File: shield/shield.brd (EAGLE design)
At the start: 102.5 x 66 mm, 4 parts, among them IC1 LM73

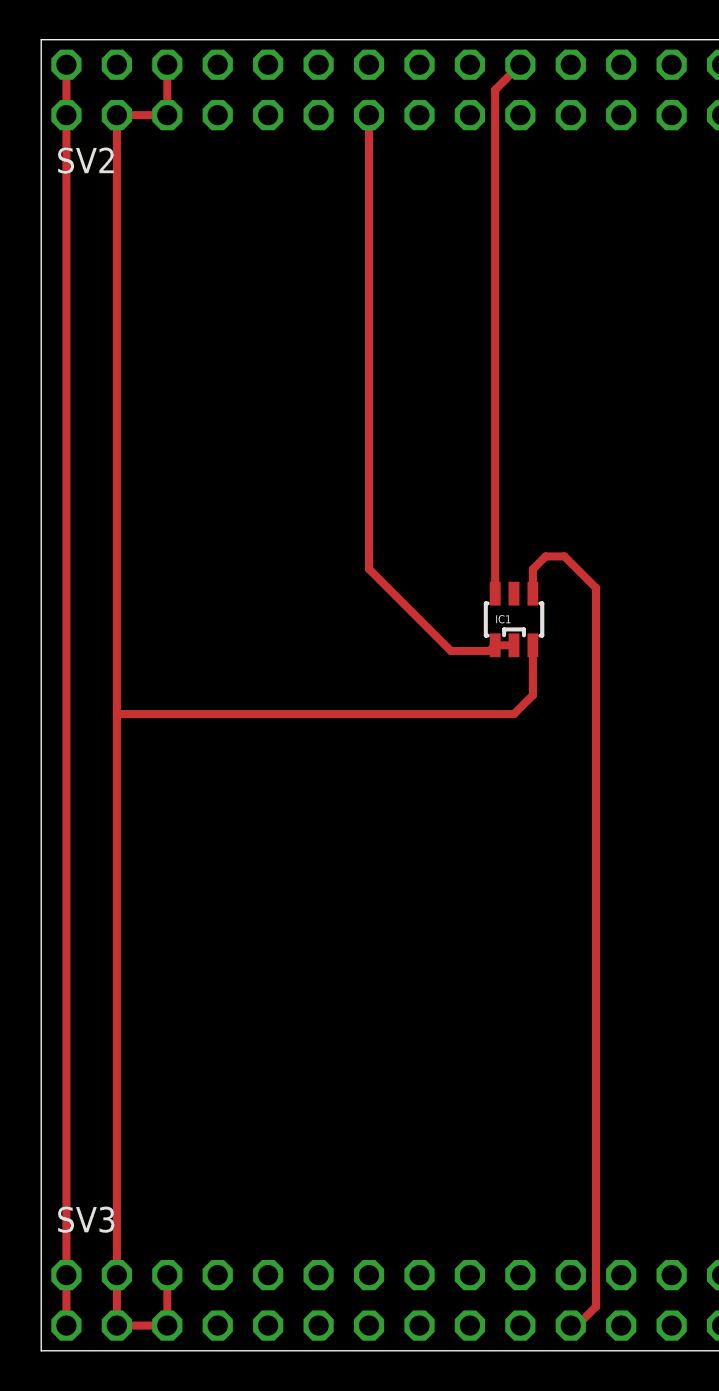
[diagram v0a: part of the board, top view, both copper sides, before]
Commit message: remove lm73 from shield
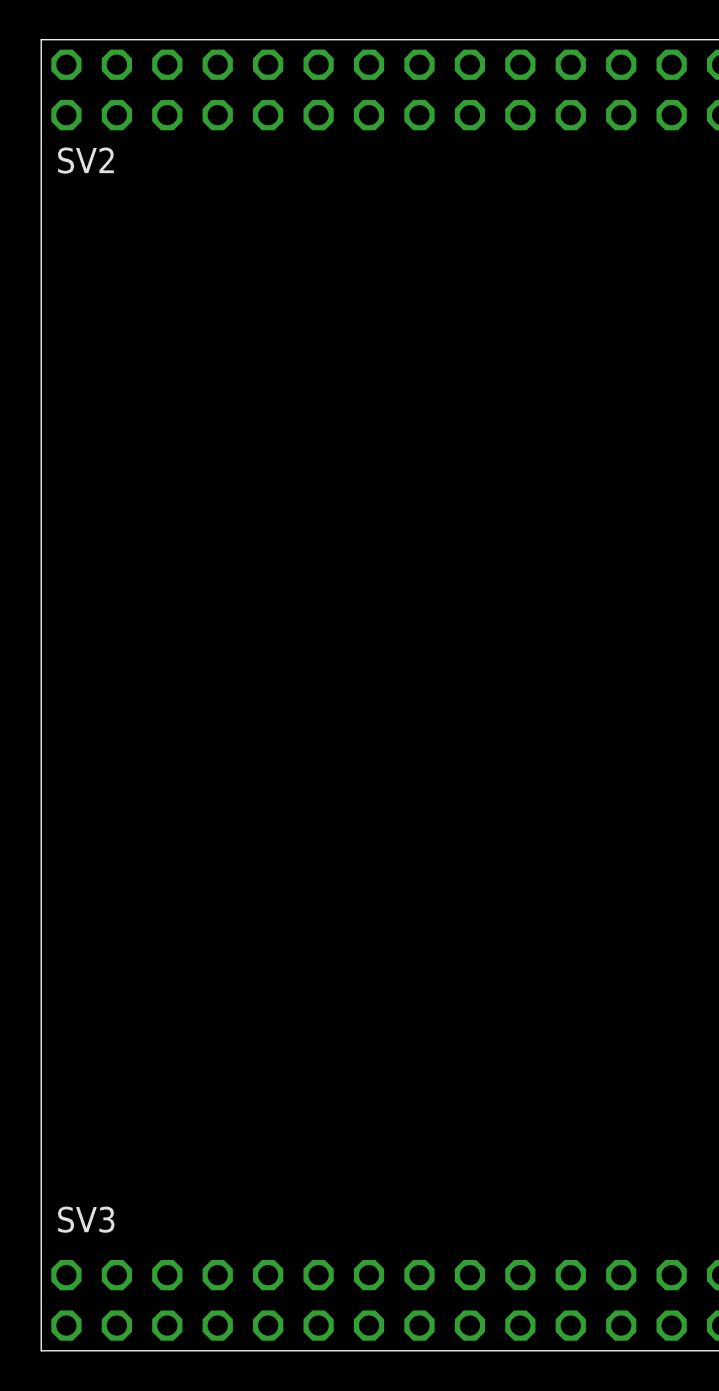
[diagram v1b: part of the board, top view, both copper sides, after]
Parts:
- removed IC1: LM73, boomerang:SOT23-6
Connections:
- net +3V3: no longer IC1.3
- net GND: no longer IC1.1, IC1.2
- net P40: no longer IC1.6
- net P41: no longer IC1.4
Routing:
- net +3V3: track 95.0 -> 0.00 mm
- net +5V: track 63.5 -> 0.00 mm
- net P41: track 43.2 -> 0.00 mm
- net GND: track 32.0 -> 0.00 mm
- net P40: track 27.2 -> 0.00 mm
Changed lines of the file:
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@@
 <attribute name="VALUE" x="93.98" y="18.161" size="1.27" layer="28" ratio="10" rot="MR180"/>
 </element>
-<element name="IC1" library="boomerang" package="SOT23-6" value="LM73" x="22.5425" y="48.26"/>
 </elements>
 <signals>
@@
 <contactref element="SV2" pad="57"/>
 <contactref element="SV2" pad="79"/>
-<contactref element="IC1" pad="1"/>
-<contactref element="IC1" pad="2"/>
 <wire x1="88.9" y1="73.66" x2="99.06" y2="76.2" width="0" layer="19" extent="1-1"/>
 <wire x1="71.12" y1="76.2" x2="88.9" y2="73.66" width="0" layer="19" extent="1-1"/>
@@
 <wire x1="43.18" y1="15.24" x2="68.58" y2="15.24" width="0" layer="19" extent="1-1"/>
 <wire x1="22.86" y1="15.24" x2="43.18" y2="15.24" width="0" layer="19" extent="1-1"/>
-<wire x1="15.24" y1="73.66" x2="15.24" y2="50.8" width="0.4064" layer="1"/>
-<wire x1="15.24" y1="50.8" x2="19.3675" y2="46.6725" width="0.4064" layer="1"/>
-<wire x1="19.3675" y1="46.6725" x2="21.3051" y2="46.6725" width="0.4064" layer="1"/>
-<wire x1="21.3051" y1="46.6725" x2="21.5925" y2="46.9599" width="0.4064" layer="1"/>
-<wire x1="21.5925" y1="46.9599" x2="22.5425" y2="46.9599" width="0.4064" layer="1"/>
 </signal>
 <signal name="P14">
@@
 <signal name="P40">
 <contactref element="SV2" pad="19"/>
-<contactref element="IC1" pad="6"/>
-<wire x1="21.5925" y1="49.5601" x2="21.5925" y2="74.9325" width="0.4064" layer="1"/>
-<wire x1="21.5925" y1="74.9325" x2="22.86" y2="76.2" width="0.4064" layer="1"/>
 </signal>
 <signal name="P36">
@@
 <signal name="P41">
 <contactref element="SV3" pad="22"/>
-<contactref element="IC1" pad="4"/>
-<wire x1="23.4925" y1="49.5601" x2="23.4925" y2="50.7975" width="0.4064" layer="1"/>
-<wire x1="23.4925" y1="50.7975" x2="24.13" y2="51.435" width="0.4064" layer="1"/>
-<wire x1="24.13" y1="51.435" x2="25.0825" y2="51.435" width="0.4064" layer="1"/>
-<wire x1="25.4" y1="12.7" x2="25.7175" y2="12.7" width="0.4064" layer="1"/>
-<wire x1="25.7175" y1="12.7" x2="26.67" y2="13.6525" width="0.4064" layer="1"/>
-<wire x1="26.67" y1="13.6525" x2="26.67" y2="49.8475" width="0.4064" layer="1"/>
-<wire x1="26.67" y1="49.8475" x2="25.0825" y2="51.435" width="0.4064" layer="1"/>
 </signal>
 <signal name="P45">
@@
 <contactref element="SV2" pad="6"/>
 <contactref element="SV2" pad="5"/>
-<wire x1="5.08" y1="76.2" x2="5.08" y2="73.66" width="0.4064" layer="1"/>
-<wire x1="5.08" y1="73.66" x2="2.54" y2="73.66" width="0.4064" layer="1"/>
-<wire x1="2.54" y1="73.66" x2="2.54" y2="43.4975" width="0.4064" layer="1"/>
-<wire x1="2.54" y1="43.4975" x2="2.54" y2="15.24" width="0.4064" layer="1"/>
-<wire x1="2.54" y1="15.24" x2="2.54" y2="12.7" width="0.4064" layer="1"/>
-<wire x1="5.08" y1="12.7" x2="2.54" y2="12.7" width="0.4064" layer="1"/>
-<wire x1="5.08" y1="12.7" x2="5.08" y2="15.24" width="0.4064" layer="1"/>
-<contactref element="IC1" pad="3"/>
-<wire x1="23.4925" y1="46.9599" x2="23.4925" y2="44.4475" width="0.4064" layer="1"/>
-<wire x1="23.4925" y1="44.4475" x2="22.5425" y2="43.4975" width="0.4064" layer="1"/>
-<wire x1="22.5425" y1="43.4975" x2="2.54" y2="43.4975" width="0.4064" layer="1"/>
+<wire x1="5.08" y1="73.66" x2="5.08" y2="76.2" width="0" layer="19" extent="1-1"/>
+<wire x1="2.54" y1="73.66" x2="5.08" y2="73.66" width="0" layer="19" extent="1-1"/>
+<wire x1="5.08" y1="15.24" x2="5.08" y2="73.66" width="0" layer="19" extent="1-1"/>
+<wire x1="5.08" y1="12.7" x2="5.08" y2="15.24" width="0" layer="19" extent="1-1"/>
+<wire x1="2.54" y1="15.24" x2="5.08" y2="15.24" width="0" layer="19" extent="1-1"/>
+<wire x1="2.54" y1="12.7" x2="5.08" y2="12.7" width="0" layer="19" extent="1-1"/>
 </signal>
 <signal name="+5V">
@@
 <contactref element="SV2" pad="1"/>
 <contactref element="SV2" pad="2"/>
-<wire x1="0" y1="76.2" x2="0" y2="73.66" width="0.4064" layer="1"/>
-<wire x1="0" y1="73.66" x2="0" y2="15.24" width="0.4064" layer="1"/>
-<wire x1="0" y1="15.24" x2="0" y2="12.7" width="0.4064" layer="1"/>
+<wire x1="0" y1="73.66" x2="0" y2="76.2" width="0" layer="19" extent="1-1"/>
+<wire x1="0" y1="15.24" x2="0" y2="73.66" width="0" layer="19" extent="1-1"/>
+<wire x1="0" y1="12.7" x2="0" y2="15.24" width="0" layer="19" extent="1-1"/>
 </signal>
 </signals>

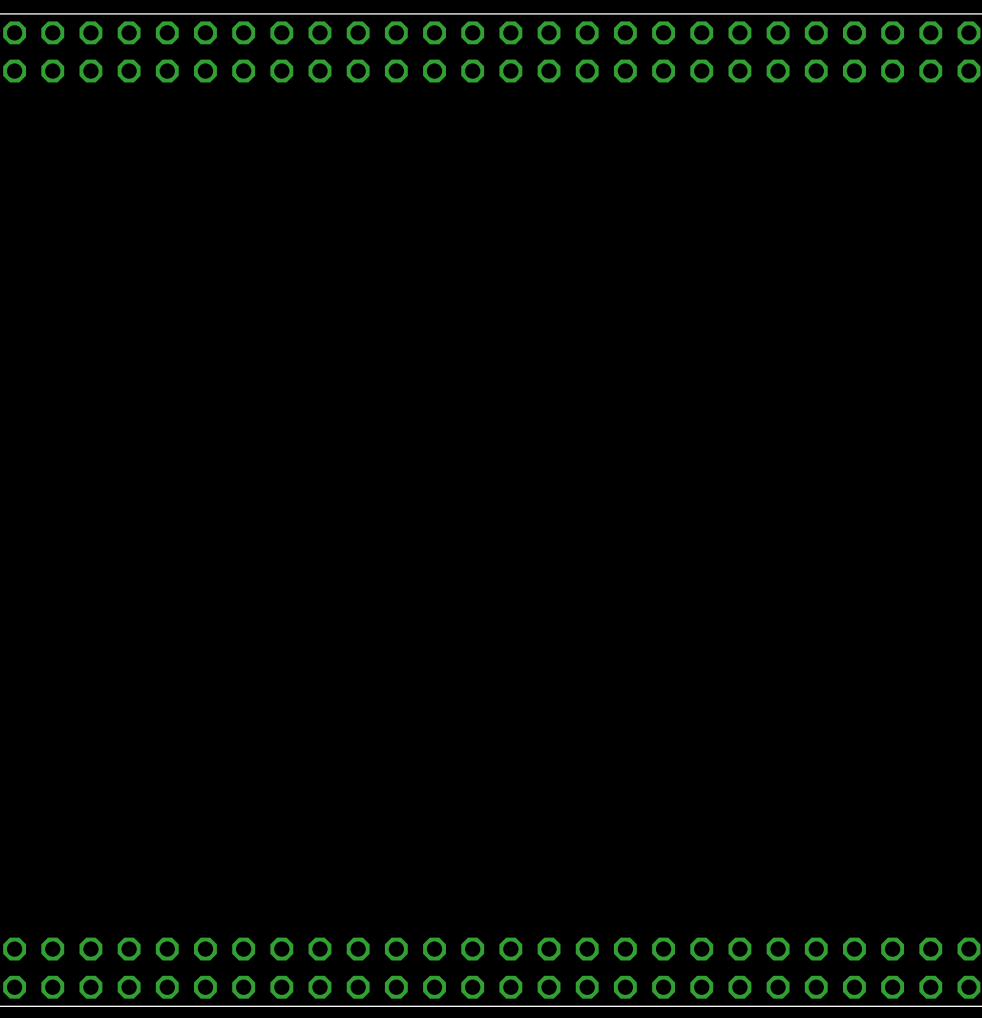
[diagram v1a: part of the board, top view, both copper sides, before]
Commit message: Update schield schematic
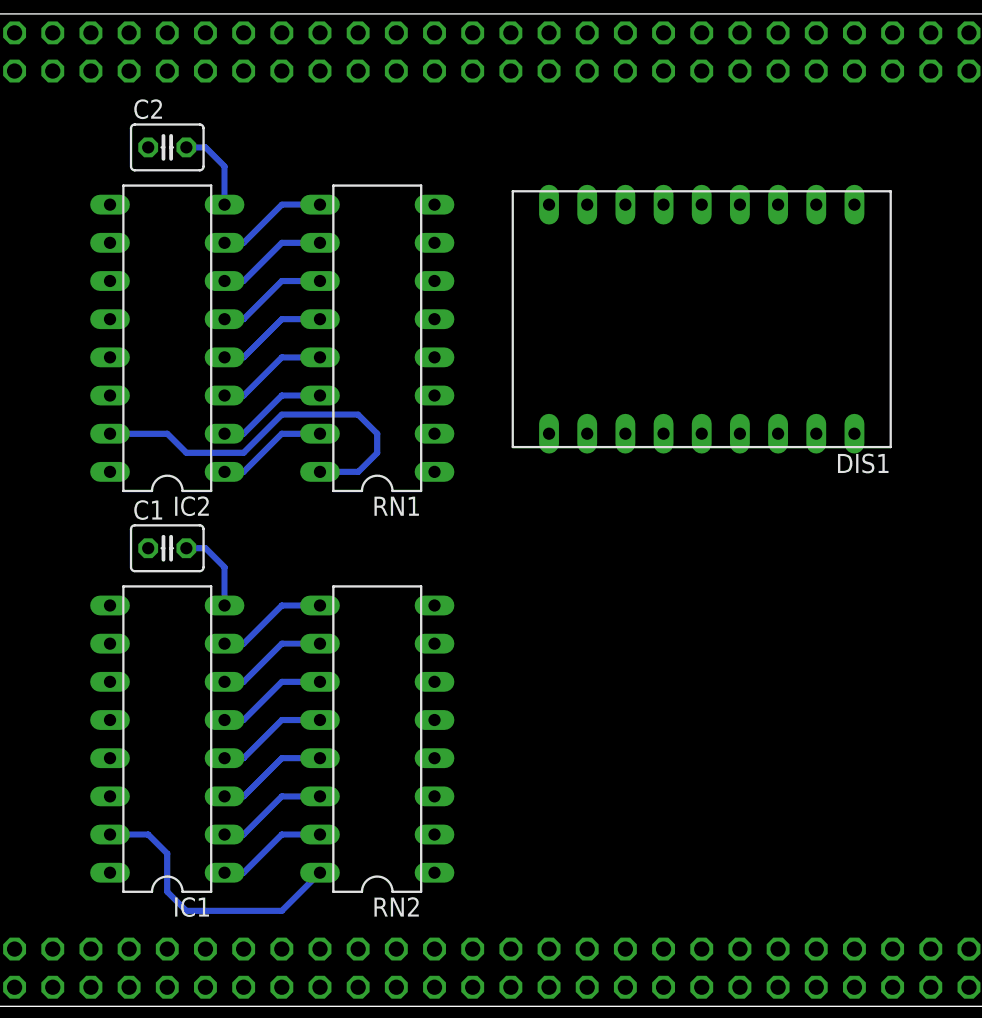
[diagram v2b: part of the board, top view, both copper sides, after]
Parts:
- added C1, C2: (no value), rcl:C025-030X050
- added DIS1: HD-K123, display-hp:HDSP-R
- added IC1, IC2: 74HC594N, 74xx-eu:DIL16
- added RN1, RN2: (no value), resistor-dil:DIL16
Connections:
- new net N$1: IC2.15, RN1.16
- new net N$10: IC1.1, RN2.15
- new net N$11: IC1.2, RN2.14
- new net N$12: IC1.3, RN2.13
- new net N$13: IC1.4, RN2.12
- new net N$14: IC1.5, RN2.11
- new net N$15: IC1.6, RN2.10
- new net N$16: IC1.7, RN2.9
- new net N$17: IC1.9, IC2.14
- new net N$18: DIS1.11, RN1.1
- new net N$19: DIS1.10, RN1.2
- new net N$2: IC2.1, RN1.15
- new net N$20: DIS1.8, RN1.3
- new net N$21: DIS1.6, RN1.4
- new net N$22: DIS1.5, RN1.5
- new net N$23: DIS1.12, RN1.6
- new net N$24: DIS1.7, RN1.7
- new net N$25: DIS1.17, RN2.7
- new net N$26: DIS1.16, RN2.1
- new net N$27: DIS1.15, RN2.2
- new net N$28: DIS1.3, RN2.3
- new net N$29: DIS1.2, RN2.4
- new net N$3: IC2.2, RN1.14
- new net N$30: DIS1.1, RN2.5
- new net N$31: DIS1.18, RN2.6
- new net N$32: DIS1.9, RN1.8
- new net N$33: DIS1.4, RN2.8
- new net N$4: IC2.3, RN1.13
- new net N$5: IC2.4, RN1.12
- new net N$6: IC2.5, RN1.11
- new net N$7: IC2.6, RN1.10
- new net N$8: IC2.7, RN1.9
- new net N$9: IC1.15, RN2.16
- net +3V3: now also C1.1, C2.1, IC1.16, IC2.16
- net GND: now also C1.2, C2.2, DIS1.13, DIS1.14, IC1.8, IC2.8
- net P15: now also IC1.10, IC1.13, IC2.10, IC2.13
- net P44: now also IC1.12, IC2.12
- net P46: now also IC1.14
- net P48: now also IC1.11, IC2.11
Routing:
- net N$1: track 0.00 -> 25.5 mm
- net N$9: track 0.00 -> 18.6 mm
- net GND: track 0.00 -> 11.2 mm
- net N$14: track 0.00 -> 7.40 mm
- net N$12: track 0.00 -> 7.40 mm
- net N$8: track 0.00 -> 7.40 mm
- net N$7: track 0.00 -> 7.40 mm
- net N$6: track 0.00 -> 7.40 mm
- net N$5: track 0.00 -> 7.40 mm
- net N$4: track 0.00 -> 7.40 mm
- net N$3: track 0.00 -> 7.40 mm
- net N$2: track 0.00 -> 7.40 mm
- net N$16: track 0.00 -> 7.40 mm
- net N$15: track 0.00 -> 7.40 mm
- net N$13: track 0.00 -> 7.40 mm
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
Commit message: Update schematic
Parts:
- removed C2: (no value), rcl:C025-030X050
- removed DIS1: HD-K123, display-hp:HDSP-R
- removed IC1, IC2: 74HC594N, 74xx-eu:DIL16
- removed RN1, RN2: (no value), resistor-dil:DIL16
- added DIS2: HD-K121, display-hp:HDSP-R
- added U1: TLC5925IDWR, Texas Instruments_By_element14_Batch_1:SOIC127P1030X265-24N
- C1: value (none) -> 100n; device rcl:C025-030X050 -> capacitor-wima:C2.5-2
- moved C1 36.1 mm to (55.9, 64.8)
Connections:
- removed net N$17: IC1.9, IC2.14
- removed net N$18: DIS1.11, RN1.1
- removed net N$19: DIS1.10, RN1.2
- removed net N$20: DIS1.8, RN1.3
- removed net N$21: DIS1.6, RN1.4
- removed net N$22: DIS1.5, RN1.5
- removed net N$23: DIS1.12, RN1.6
- removed net N$24: DIS1.7, RN1.7
- removed net N$25: DIS1.17, RN2.7
- removed net N$26: DIS1.16, RN2.1
- removed net N$27: DIS1.15, RN2.2
- removed net N$28: DIS1.3, RN2.3
- removed net N$29: DIS1.2, RN2.4
- removed net N$30: DIS1.1, RN2.5
- removed net N$31: DIS1.18, RN2.6
- removed net N$32: DIS1.9, RN1.8
- removed net N$33: DIS1.4, RN2.8
- net +3V3: now also DIS2.13, DIS2.14, U1.24; no longer C2.1, IC1.16, IC2.16
- net GND: now also U1.1; no longer C2.2, DIS1.13, DIS1.14, IC1.8, IC2.8
- net N$1: now also DIS2.5, U1.5; no longer IC2.15, RN1.16
- net N$10: now also DIS2.2, U1.14; no longer IC1.1, RN2.15
- net N$11: now also DIS2.17, U1.15; no longer IC1.2, RN2.14
- net N$12: now also DIS2.3, U1.16; no longer IC1.3, RN2.13
- net N$13: now also DIS2.4, U1.17; no longer IC1.4, RN2.12
- net N$14: now also DIS2.15, U1.18; no longer IC1.5, RN2.11
- net N$15: now also DIS2.16, U1.19; no longer IC1.6, RN2.10
- net N$16: now also DIS2.18, U1.20; no longer IC1.7, RN2.9
- net N$2: now also DIS2.6, U1.6; no longer IC2.1, RN1.15
- net N$3: now also DIS2.7, U1.7; no longer IC2.2, RN1.14
- net N$4: now also DIS2.8, U1.8; no longer IC2.3, RN1.13
- net N$5: now also DIS2.9, U1.9; no longer IC2.4, RN1.12
- net N$6: now also DIS2.10, U1.10; no longer IC2.5, RN1.11
- net N$7: now also DIS2.11, U1.11; no longer IC2.6, RN1.10
- net N$8: now also DIS2.12, U1.12; no longer IC2.7, RN1.9
- net N$9: now also DIS2.1, U1.13; no longer IC1.15, RN2.16
- net P15: no longer IC1.10, IC1.13, IC2.10, IC2.13
- net P44: no longer IC1.12, IC2.12
- net P46: now also U1.2; no longer IC1.14
- net P48: now also U1.3; no longer IC1.11, IC2.11
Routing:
- net +3V3: track 0.00 -> 80.7 mm
- net N$11: track 7.40 -> 84.1 mm
- net N$13: track 7.40 -> 69.3 mm
- net N$2: track 7.40 -> 64.2 mm
- net N$12: track 7.40 -> 60.4 mm
- net N$3: track 7.40 -> 55.3 mm
- net N$1: track 25.5 -> 73.1 mm
- net N$4: track 7.40 -> 46.4 mm
- net N$10: track 7.40 -> 45.2 mm
- net N$16: track 7.40 -> 41.1 mm
- net N$5: track 7.40 -> 32.5 mm
- net N$15: track 7.40 -> 25.3 mm
- net N$9: track 18.6 -> 36.3 mm
- net GND: track 11.2 -> 0.00 mm
- net N$14: track 7.40 -> 12.8 mm
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
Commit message: Update schematics
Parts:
- added IC1: LM75, lm75:SO8_LM75
- added Q1, Q2, Q3, Q4: BUZ11BV, transistor-power:TO220BV
- added R1, R2: 10k, rcl:0207/10
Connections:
- new net N$17: Q1.S, Q2.S, Q3.S, Q4.S
- net +3V3: now also IC1.8, R1.2, R2.2
- net GND: now also IC1.4, IC1.5, IC1.6, IC1.7
- net P40: now also IC1.1, R2.1
- net P41: now also IC1.2, R1.1
- net P77: now also Q1.G
- net P78: now also Q2.G
- net P79: now also Q3.G
- net P80: now also Q4.G
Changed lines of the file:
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@@
 </element>
 <element name="C1" library="capacitor-wima" package="C2.5-2" value="100n" x="55.88" y="64.77"/>
+<element name="Q1" library="transistor-power" package="TO220BV" value="BUZ11BV" x="5.08" y="10.16"/>
+<element name="Q2" library="transistor-power" package="TO220BV" value="BUZ11BV" x="5.08" y="1.27"/>
+<element name="Q3" library="transistor-power" package="TO220BV" value="BUZ11BV" x="5.08" y="-7.62"/>
+<element name="Q4" library="transistor-power" package="TO220BV" value="BUZ11BV" x="5.08" y="-16.51"/>
+<element name="IC1" library="lm75" package="SO8_LM75" value="LM75" x="3.81" y="-29.21"/>
+<element name="R1" library="rcl" package="0207/10" value="10k" x="5.08" y="-36.83"/>
+<element name="R2" library="rcl" package="0207/10" value="10k" x="5.08" y="-41.91"/>
 </elements>
 <signals>
@@
 <contactref element="U1" pad="1"/>
 <contactref element="C1" pad="2"/>
+<contactref element="IC1" pad="4"/>
+<contactref element="IC1" pad="5"/>
+<contactref element="IC1" pad="6"/>
+<contactref element="IC1" pad="7"/>
 <wire x1="88.9" y1="73.66" x2="99.06" y2="76.2" width="0" layer="19" extent="1-1"/>
 <wire x1="71.12" y1="76.2" x2="88.9" y2="73.66" width="0" layer="19" extent="1-1"/>
@@
 <wire x1="43.18" y1="15.24" x2="68.58" y2="15.24" width="0" layer="19" extent="1-1"/>
 <wire x1="22.86" y1="15.24" x2="43.18" y2="15.24" width="0" layer="19" extent="1-1"/>
+<wire x1="6.35" y1="-26.035" x2="22.86" y2="15.24" width="0" layer="19" extent="1-1"/>
+<wire x1="5.08" y1="-26.035" x2="6.35" y2="-26.035" width="0" layer="19" extent="1-1"/>
+<wire x1="3.81" y1="-26.035" x2="5.08" y2="-26.035" width="0" layer="19" extent="1-1"/>
+<wire x1="6.35" y1="-32.385" x2="6.35" y2="-26.035" width="0" layer="19" extent="1-1"/>
 </signal>
 <signal name="P14">
@@
 <signal name="P78">
 <contactref element="SV2" pad="40"/>
+<contactref element="Q2" pad="G"/>
+<wire x1="2.54" y1="-1.27" x2="48.26" y2="73.66" width="0" layer="19" extent="1-1"/>
 </signal>
 <signal name="P86">
@@
 <signal name="P80">
 <contactref element="SV2" pad="39"/>
+<contactref element="Q4" pad="G"/>
+<wire x1="2.54" y1="-19.05" x2="48.26" y2="76.2" width="0" layer="19" extent="1-1"/>
 </signal>
 <signal name="P76">
@@
 <signal name="P40">
 <contactref element="SV2" pad="19"/>
+<contactref element="IC1" pad="1"/>
+<contactref element="R2" pad="1"/>
+<wire x1="2.54" y1="-32.385" x2="22.86" y2="76.2" width="0" layer="19" extent="1-1"/>
+<wire x1="0" y1="-41.91" x2="2.54" y2="-32.385" width="0" layer="19" extent="1-1"/>
 </signal>
 <signal name="P36">
@@
 <signal name="P41">
 <contactref element="SV3" pad="22"/>
+<contactref element="IC1" pad="2"/>
+<contactref element="R1" pad="1"/>
+<wire x1="3.81" y1="-32.385" x2="25.4" y2="12.7" width="0" layer="19" extent="1-1"/>
+<wire x1="0" y1="-36.83" x2="3.81" y2="-32.385" width="0" layer="19" extent="1-1"/>
 </signal>
 <signal name="P45">
@@
 <signal name="P77">
 <contactref element="SV3" pad="40"/>
+<contactref element="Q1" pad="G"/>
+<wire x1="2.54" y1="7.62" x2="48.26" y2="12.7" width="0" layer="19" extent="1-1"/>
 </signal>
 <signal name="P81">
@@
 <signal name="P79">
 <contactref element="SV3" pad="39"/>
+<contactref element="Q3" pad="G"/>
+<wire x1="2.54" y1="-10.16" x2="48.26" y2="15.24" width="0" layer="19" extent="1-1"/>
 </signal>
 <signal name="P83">
@@
 <wire x1="54.61" y1="60.96" x2="58.42" y2="57.15" width="0.4064" layer="16"/>
 <wire x1="58.42" y1="57.15" x2="58.42" y2="41.91" width="0.4064" layer="16"/>
+<contactref element="R1" pad="2"/>
+<contactref element="R2" pad="2"/>
+<contactref element="IC1" pad="8"/>
 <wire x1="5.08" y1="73.66" x2="5.08" y2="76.2" width="0" layer="19" extent="1-1"/>
 <wire x1="2.54" y1="73.66" x2="5.08" y2="73.66" width="0" layer="19" extent="1-1"/>
@@
 <wire x1="2.54" y1="15.24" x2="5.08" y2="15.24" width="0" layer="19" extent="1-1"/>
 <wire x1="2.54" y1="12.7" x2="5.08" y2="12.7" width="0" layer="19" extent="1-1"/>
+<wire x1="2.54" y1="-26.035" x2="2.54" y2="12.7" width="0" layer="19" extent="1-1"/>
+<wire x1="10.16" y1="-36.83" x2="2.54" y2="-26.035" width="0" layer="19" extent="1-1"/>
+<wire x1="10.16" y1="-41.91" x2="10.16" y2="-36.83" width="0" layer="19" extent="1-1"/>
 </signal>
 <signal name="+5V">
@@
 <wire x1="63.5" y1="46.99" x2="63.5" y2="41.91" width="0.4064" layer="16"/>
 </signal>
+<signal name="N$17">
+<contactref element="Q1" pad="S"/>
+<contactref element="Q2" pad="S"/>
+<contactref element="Q3" pad="S"/>
+<contactref element="Q4" pad="S"/>
+<wire x1="7.62" y1="-1.27" x2="7.62" y2="7.62" width="0" layer="19" extent="1-1"/>
+<wire x1="7.62" y1="-10.16" x2="7.62" y2="-1.27" width="0" layer="19" extent="1-1"/>
+<wire x1="7.62" y1="-19.05" x2="7.62" y2="-10.16" width="0" layer="19" extent="1-1"/>
+</signal>
 </signals>
